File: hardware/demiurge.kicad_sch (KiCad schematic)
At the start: 127 parts, among them J12 Micro_SD_Card_Det_Hirose_DM3AT, J2 Conn_01x06, U1 MCP6002, U10 TL072, U11 TL072, U13 CH32V307RCT6, U2 AMS1117-3.3, U3 MCP6002, U4 AW9523BTQR, U5 W25Q128JVS, U6 74LVC1T45W6, U7 TL072, U8 TL072, Y1 16MHz

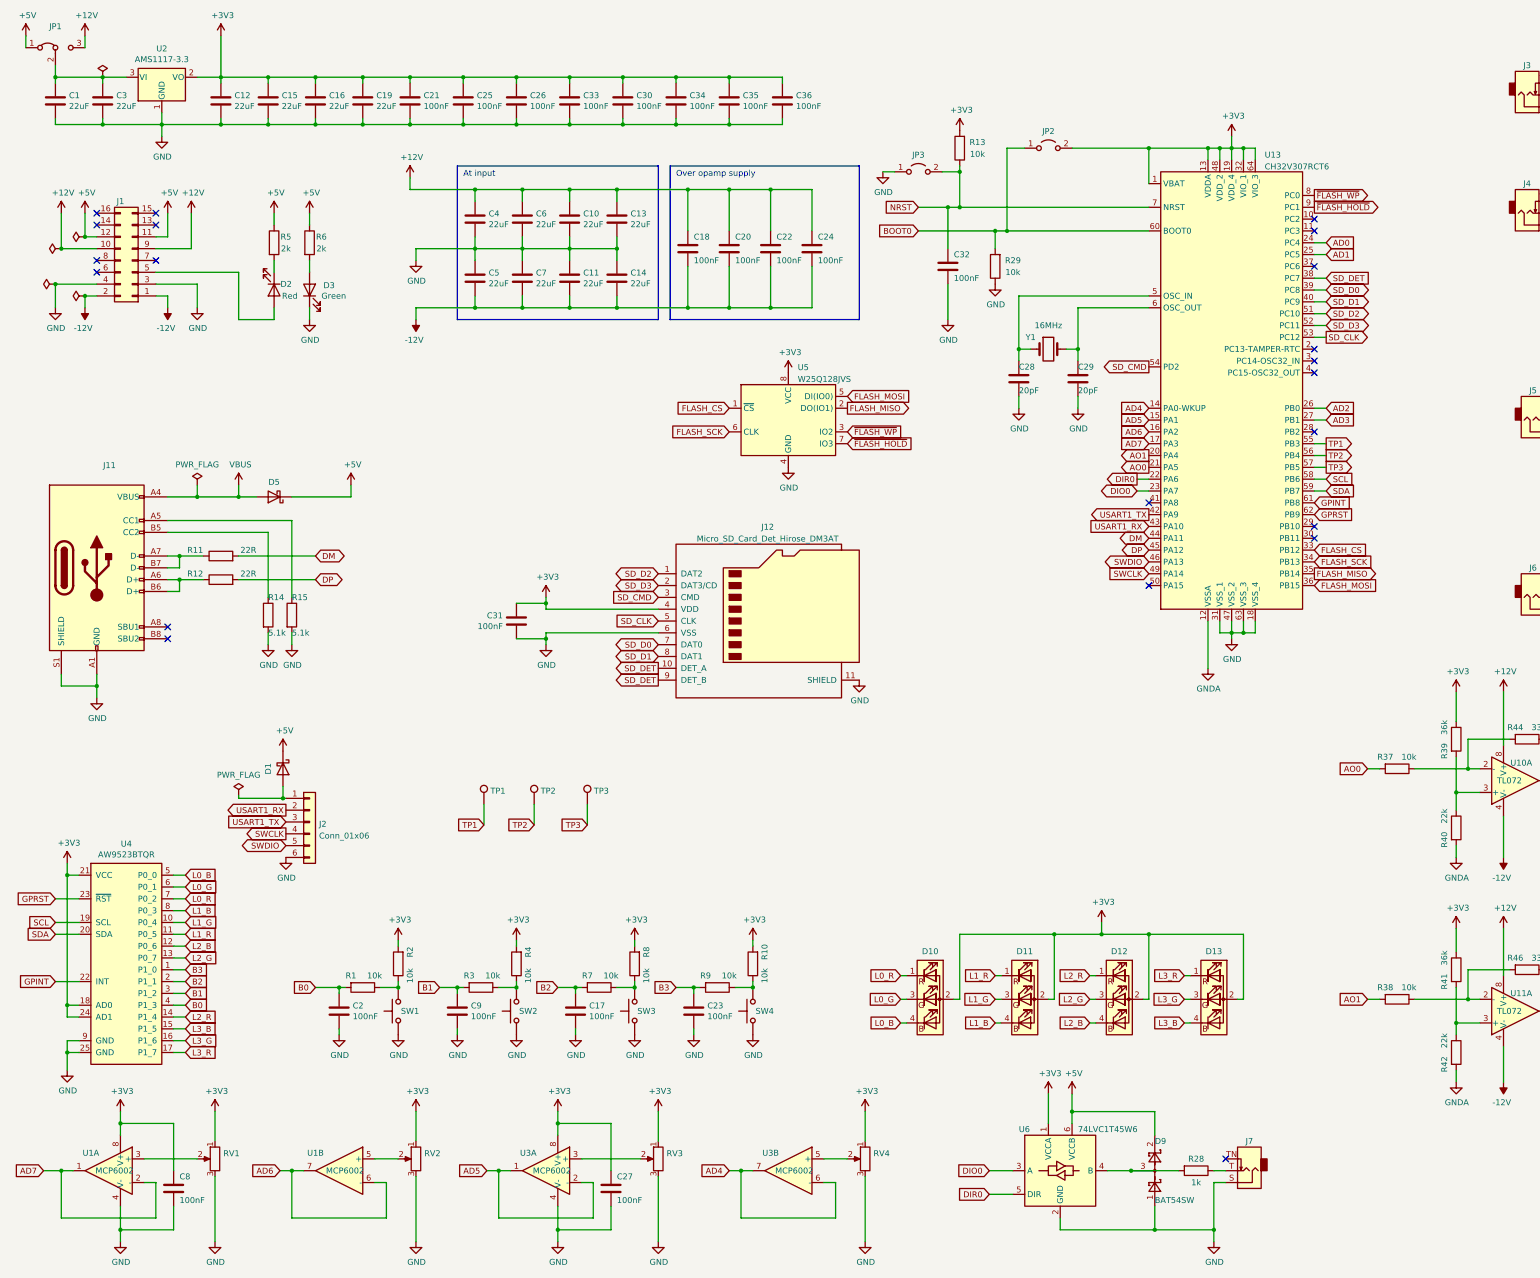
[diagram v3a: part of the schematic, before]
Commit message: AW9523 is discontinued @ LCSC. Changing to AW20036, capable of up to 12 RGB LEDs.
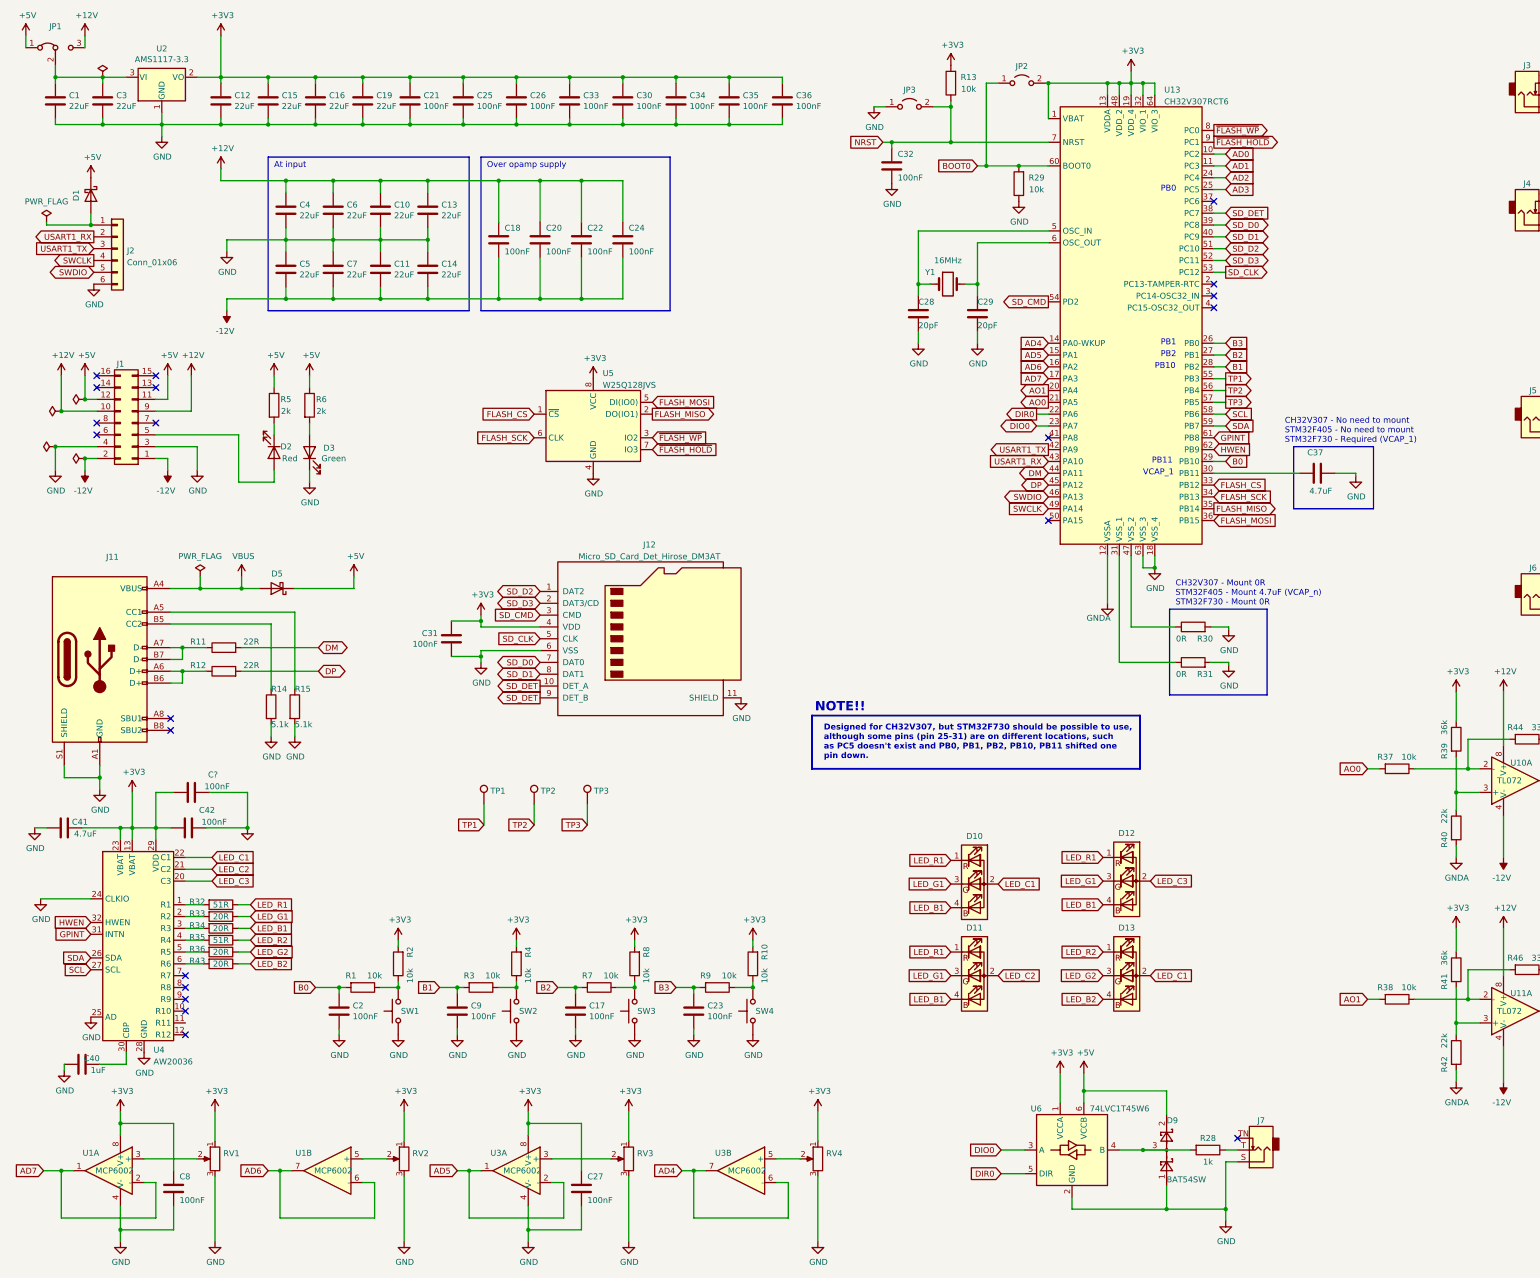
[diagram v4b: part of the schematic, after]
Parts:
- removed U4: AW9523BTQR, Package_DFN_QFN:VQFN-24-1EP_4x4mm_P0.5mm_EP2.45x2.45mm, symbol aaa:AW9523BTQR
- added C37, C41: 4.7uF, Capacitor_SMD:C_0805_2012Metric, symbol Device:C
- added C40: 1uF, Capacitor_SMD:C_0603_1608Metric, symbol Device:C
- added C42, C?: 100nF, Capacitor_SMD:C_0603_1608Metric, symbol Device:C
- added R30, R31: 0R, Capacitor_SMD:C_0603_1608Metric, symbol Device:R
- added R32, R35: 51R, Resistor_SMD:R_0603_1608Metric, symbol Device:R
- added R33, R34, R36, R43: 20R, Resistor_SMD:R_0603_1608Metric, symbol Device:R
- added U4: AW20036, symbol awesomeaudio:AW20036
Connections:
- net L1_B is gone; now on net LED_B1: D11.4 (BK)
- net L1_G is gone; now on net LED_G1: D11.3 (GK)
- net L1_R is gone; now on net LED_R1: D11.1 (RK)
- net L2_B is gone; now on net LED_B1: D12.4 (BK)
- net L2_G is gone; now on net LED_G1: D12.3 (GK)
- net L2_R is gone; now on net LED_R1: D12.1 (RK)
- net +3V3: now also C41.2, C42.1, C?.1, U4.13 (VBAT), U4.23 (VBAT), U4.29 (VDD); no longer D10.2 (A), D11.2 (A), D12.2 (A), D13.2 (A)
- net AD0: now also U13.10 (PC2); no longer U13.24 (PC4)
- net AD1: now also U13.11 (PC3); no longer U13.25 (PC5)
- net AD2: now also U13.24 (PC4); no longer U13.26 (PB0)
- net AD3: now also U13.25 (PC5); no longer U13.27 (PB1)
- net B0: now also U13.29 (PB10)
- net B1: now also U13.28 (PB2)
- net B2: now also U13.27 (PB1)
- net B3: now also U13.26 (PB0)
- net GND: now also C37.2, C40.1, C41.1, C42.2, C?.2, R30.2, R31.2, U4.24 (CLKIO), U4.25 (AD), U4.28 (GND); no longer U13.31 (VSS_1), U13.47 (VSS_2)
- net GPINT: now also U4.31 (INTN)
- net SCL: now also U4.27 (SCL)
- net SDA: now also U4.26 (SDA)
- net at U13.30 (PB11): now also C37.1
- net GPRST renamed HWEN
- net HWEN: now also U4.32 (HWEN)
- net L0_B renamed LED_B1
- net LED_B1: now also R34.1
- net L0_G renamed LED_G1
- net LED_G1: now also R33.1
- net L0_R renamed LED_R1
- net LED_R1: now also R32.1
- net L3_B renamed LED_B2
- net LED_B2: now also R43.1
- net L3_G renamed LED_G2
- net LED_G2: now also R36.1
- net L3_R renamed LED_R2
- net LED_R2: now also R35.1
- new net: R33.2, U4.2 (R2)
- new net: R35.2, U4.4 (R4)
- new net: R30.1, U13.47 (VSS_2)
- new net: R32.2, U4.1 (R1)
- new net: R34.2, U4.3 (R3)
- new net: C40.2, U4.30 (CBP)
- new net: R36.2, U4.5 (R5)
- new net: R43.2, U4.6 (R6)
- new net: R31.1, U13.31 (VSS_1)
- new net LED_C1: D10.2 (A), D13.2 (A), U4.22 (C1)
- new net LED_C2: D11.2 (A), U4.21 (C2)
- new net LED_C3: D12.2 (A), U4.20 (C3)
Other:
- note added: "CH32V307 - Mount 0R STM32F405 - Mount 4.7uF (VCAP_n) STM32F730 - Mount 0R"
- note added: "CH32V307 - No need to mount STM32F405 - No need to mount STM32F730 - Required (VCAP_1)"
- note added: "Designed for CH32V307, but STM32F730 should be possible to use, although some pins (pin 25-31) are on different locations, such as PC5 doesn't exist and PB0, PB1, PB2, PB10, PB11 shifted one pin down."
- note added: "NOTE!!"
- note added: "PB0"
- note added: "PB1"
- note added: "PB10"
- note added: "PB11"
- note added: "PB2"
- note added: "VCAP_1"
- moved on the sheet: C10, C11, C13, C14, C18, C20, C22, C24, C27, C28, C29, C31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
